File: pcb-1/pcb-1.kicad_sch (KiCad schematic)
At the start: 6 parts, among them J1 Raspberry_Pi_2_3, J2 Screw_Terminal_01x03, J3 Conn_01x07_Socket, J4 Screw_Terminal_01x02, U1 Pico

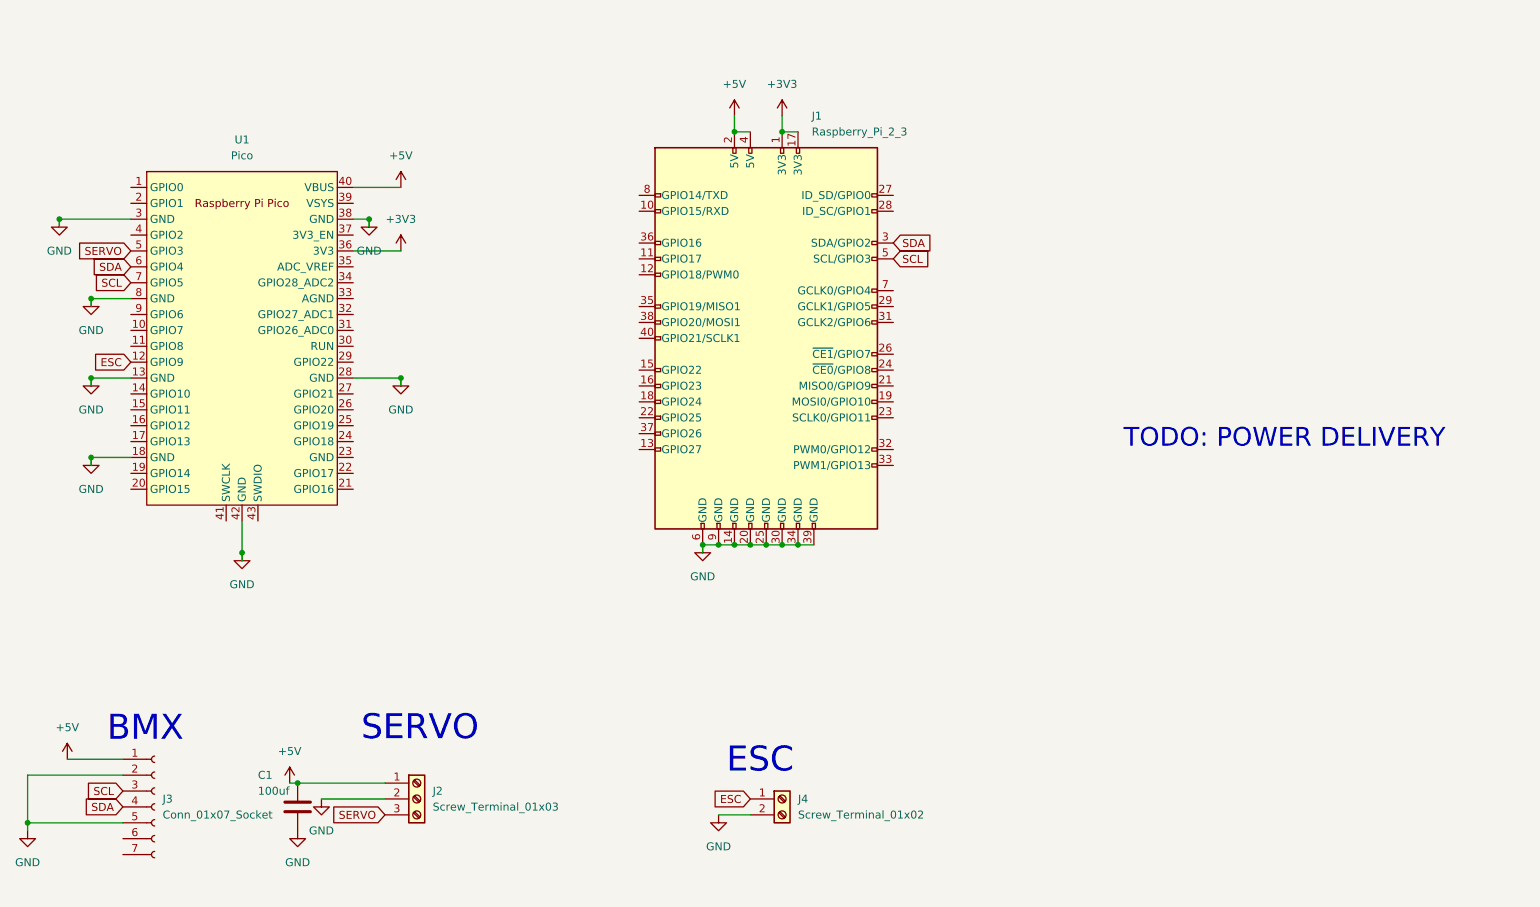
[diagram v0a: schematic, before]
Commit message: updated directory naming, completed routing? (still unsure about decoupling cap location)
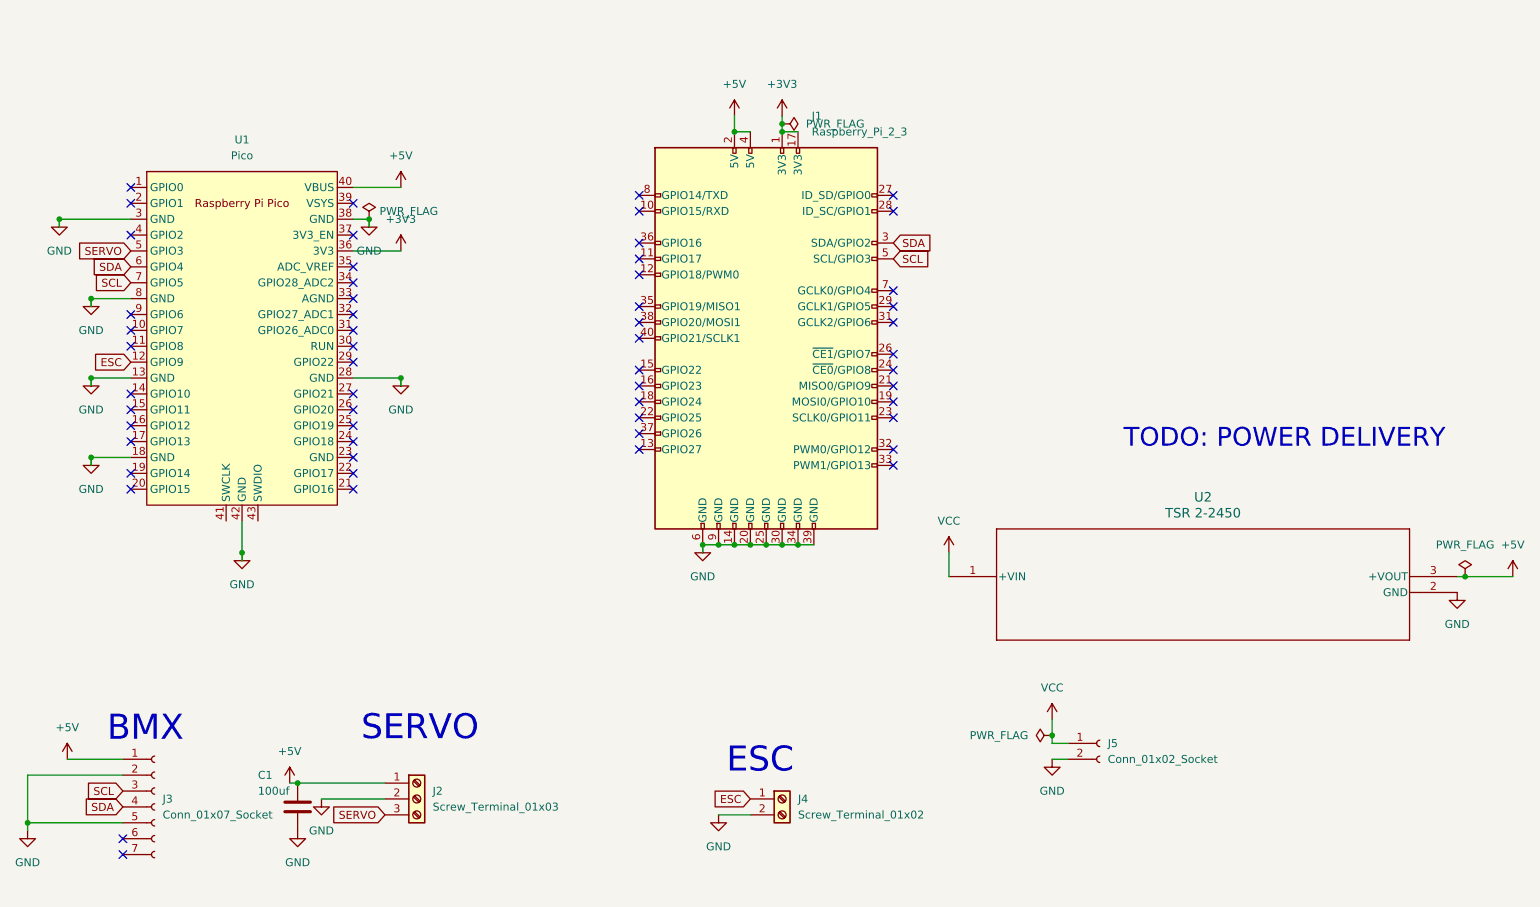
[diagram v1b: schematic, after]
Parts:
- added J5: Conn_01x02_Socket, Connector_AMASS:AMASS_XT60-F_1x02_P7.20mm_Vertical, symbol Connector:Conn_01x02_Socket
- added U2: TSR 2-2450, txr:TSR 2-2450_TRP, symbol txr:TSR_2-2450
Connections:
- net +5V: now also U2.3 (+VOUT)
- net GND: now also J5.2 (Pin_2), U2.2 (GND)
- new net VCC: J5.1 (Pin_1), U2.1 (+VIN)
- no-connect marks 0 -> 56

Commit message: removed bad 3v3 net, adjusted dimensions
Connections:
- removed net +3V3: J1.1 (3V3), J1.17 (3V3), U1.36 (3V3)
- no-connect marks 56 -> 59
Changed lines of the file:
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@@
   (junction (at 54.61 109.22) (diameter 0) (color 0 0 0 0)
   )
-  (junction (at 165.1 55.88) (diameter 0) (color 0 0 0 0)
-  )
   (junction (at 162.56 123.19) (diameter 0) (color 0 0 0 0)
   )
@@
   (junction (at 78.74 124.46) (diameter 0) (color 0 0 0 0)
   )
-  (junction (at 165.1 57.15) (diameter 0) (color 0 0 0 0)
-  )
   (junction (at 160.02 123.19) (diameter 0) (color 0 0 0 0)
   )
@@
   )
   (no_connect (at 96.52 109.22))
+  (no_connect (at 165.1 57.15))
   (no_connect (at 60.96 73.66))
   (no_connect (at 142.24 105.41))
@@
   (no_connect (at 60.96 86.36))
   (no_connect (at 60.96 99.06))
+  (no_connect (at 96.52 76.2))
   (no_connect (at 96.52 91.44))
+  (no_connect (at 167.64 57.15))
   (no_connect (at 60.96 104.14))
   (no_connect (at 182.88 85.09))
@@
     (stroke (width 0) (type default))
   )
-  (wire (pts (xy 165.1 54.61) (xy 165.1 55.88))
-    (stroke (width 0) (type default))
-  )
   (wire (pts (xy 152.4 123.19) (xy 154.94 123.19))
     (stroke (width 0) (type default))
@@
     (stroke (width 0) (type default))
   )
-  (wire (pts (xy 165.1 55.88) (xy 165.1 57.15))
-    (stroke (width 0) (type default))
-  )
-  (wire (pts (xy 96.52 76.2) (xy 104.14 76.2))
-    (stroke (width 0) (type default))
-  )
   (wire (pts (xy 96.52 71.12) (xy 99.06 71.12))
-    (stroke (width 0) (type default))
-  )
-  (wire (pts (xy 165.1 57.15) (xy 167.64 57.15))
     (stroke (width 0) (type default))
   )
@@
     )
   )
-  (symbol (lib_id "power:+3V3") (at 165.1 54.61 0) (unit 1)
-    (in_bom yes) (on_board yes) (dnp no) (fields_autoplaced)
-    (property "Reference" "#PWR012" (at 165.1 58.42 0)
-      (effects (font (size 1.27 1.27)) hide)
-    )
-    (property "Value" "+3V3" (at 165.1 49.53 0)
-      (effects (font (size 1.27 1.27)))
-    )
-    (property "Footprint" "" (at 165.1 54.61 0)
-      (effects (font (size 1.27 1.27)) hide)
-    )
-    (property "Datasheet" "" (at 165.1 54.61 0)
-      (effects (font (size 1.27 1.27)) hide)
-    )
-    (pin "1")
-    (instances
-      (project "pcb-1"
-        (path "/43486df0-1e41-4516-8027-8058a2e1c66f"
-          (reference "#PWR012") (unit 1)
-        )
-      )
-    )
-  )
   (symbol (lib_id "power:VCC") (at 191.77 124.46 0) (unit 1)
     (in_bom yes) (on_board yes) (dnp no) (fields_autoplaced)
@@
     )
   )
-  (symbol (lib_id "power:+3V3") (at 104.14 76.2 0) (unit 1)
-    (in_bom yes) (on_board yes) (dnp no) (fields_autoplaced)
-    (property "Reference" "#PWR01" (at 104.14 80.01 0)
-      (effects (font (size 1.27 1.27)) hide)
-    )
-    (property "Value" "+3V3" (at 104.14 71.12 0)
-      (effects (font (size 1.27 1.27)))
-    )
-    (property "Footprint" "" (at 104.14 76.2 0)
-      (effects (font (size 1.27 1.27)) hide)
-    )
-    (property "Datasheet" "" (at 104.14 76.2 0)
-      (effects (font (size 1.27 1.27)) hide)
-    )
-    (pin "1")
-    (instances
-      (project "pcb-1"
-        (path "/43486df0-1e41-4516-8027-8058a2e1c66f"
-          (reference "#PWR01") (unit 1)
-        )
-      )
-    )
-  )
   (symbol (lib_id "power:VCC") (at 208.28 151.13 0) (unit 1)
     (in_bom yes) (on_board yes) (dnp no) (fields_autoplaced)
@@
         (path "/43486df0-1e41-4516-8027-8058a2e1c66f"
           (reference "#PWR04") (unit 1)
-        )
-      )
-    )
-  )
-  (symbol (lib_id "power:PWR_FLAG") (at 165.1 55.88 270) (unit 1)
-    (in_bom yes) (on_board yes) (dnp no) (fields_autoplaced)
-    (property "Reference" "#FLG02" (at 167.005 55.88 0)
-      (effects (font (size 1.27 1.27)) hide)
-    )
-    (property "Value" "PWR_FLAG" (at 168.91 55.88 90)
-      (effects (font (size 1.27 1.27)) (justify left))
-    )
-    (property "Footprint" "" (at 165.1 55.88 0)
-      (effects (font (size 1.27 1.27)) hide)
-    )
-    (property "Datasheet" "~" (at 165.1 55.88 0)
-      (effects (font (size 1.27 1.27)) hide)
-    )
-    (pin "1")
-    (instances
-      (project "pcb-1"
-        (path "/43486df0-1e41-4516-8027-8058a2e1c66f"
-          (reference "#FLG02") (unit 1)
         )
       )
@@
     )
     (property "Value" "GND" (at 99.06 76.2 0)
-      (effects (font (size 1.27 1.27)))
+      (effects (font (size 1.27 1.27)) hide)
     )
     (property "Footprint" "" (at 99.06 71.12 0)

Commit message: updates to pcb
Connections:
- net +5V: now also J3.7 (Pin_7); no longer J3.1 (Pin_1)
- net GND: now also J3.3 (Pin_3), J3.6 (Pin_6); no longer J3.2 (Pin_2), J3.5 (Pin_5)
- net SCL: now also J3.5 (Pin_5); no longer J3.3 (Pin_3)
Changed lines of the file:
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@@
   (junction (at 54.61 83.82) (diameter 0) (color 0 0 0 0)
   )
-  (junction (at 44.45 167.64) (diameter 0) (color 0 0 0 0)
-  )
   (junction (at 99.06 71.12) (diameter 0) (color 0 0 0 0)
   )
@@
   )
   (junction (at 274.32 128.27) (diameter 0) (color 0 0 0 0)
+  )
+  (junction (at 44.45 170.18) (diameter 0) (color 0 0 0 0)
   )
   (junction (at 167.64 123.19) (diameter 0) (color 0 0 0 0)
@@
   (no_connect (at 142.24 105.41))
   (no_connect (at 96.52 111.76))
+  (no_connect (at 59.69 157.48))
   (no_connect (at 182.88 69.85))
   (no_connect (at 142.24 69.85))
@@
   (no_connect (at 142.24 97.79))
   (no_connect (at 60.96 86.36))
+  (no_connect (at 59.69 160.02))
   (no_connect (at 60.96 99.06))
   (no_connect (at 96.52 76.2))
@@
   (no_connect (at 142.24 77.47))
   (no_connect (at 142.24 85.09))
-  (no_connect (at 59.69 172.72))
   (no_connect (at 96.52 78.74))
   (no_connect (at 182.88 107.95))
@@
   (no_connect (at 142.24 87.63))
   (no_connect (at 96.52 114.3))
-  (no_connect (at 59.69 170.18))
   (no_connect (at 142.24 100.33))
   (no_connect (at 142.24 67.31))
@@
     (stroke (width 0) (type default))
   )
-  (wire (pts (xy 50.8 157.48) (xy 59.69 157.48))
-    (stroke (width 0) (type default))
-  )
   (wire (pts (xy 96.52 66.04) (xy 104.14 66.04))
     (stroke (width 0) (type default))
   )
-  (wire (pts (xy 44.45 160.02) (xy 59.69 160.02))
-    (stroke (width 0) (type default))
-  )
   (wire (pts (xy 152.4 123.19) (xy 152.4 124.46))
     (stroke (width 0) (type default))
@@
     (stroke (width 0) (type default))
   )
-  (wire (pts (xy 44.45 160.02) (xy 44.45 167.64))
-    (stroke (width 0) (type default))
-  )
   (wire (pts (xy 99.06 71.12) (xy 99.06 72.39))
     (stroke (width 0) (type default))
   )
-  (wire (pts (xy 44.45 167.64) (xy 59.69 167.64))
+  (wire (pts (xy 44.45 170.18) (xy 59.69 170.18))
     (stroke (width 0) (type default))
   )
@@
     (stroke (width 0) (type default))
   )
-  (wire (pts (xy 44.45 168.91) (xy 44.45 167.64))
+  (wire (pts (xy 44.45 172.72) (xy 44.45 170.18))
     (stroke (width 0) (type default))
   )
@@
     (stroke (width 0) (type default))
   )
+  (wire (pts (xy 44.45 162.56) (xy 44.45 170.18))
+    (stroke (width 0) (type default))
+  )
   (wire (pts (xy 273.05 128.27) (xy 274.32 128.27))
     (stroke (width 0) (type default))
@@
     (stroke (width 0) (type default))
   )
+  (wire (pts (xy 59.69 177.8) (xy 59.69 172.72))
+    (stroke (width 0) (type default))
+  )
+  (wire (pts (xy 44.45 162.56) (xy 59.69 162.56))
+    (stroke (width 0) (type default))
+  )
   (wire (pts (xy 191.77 124.46) (xy 191.77 128.27))
+    (stroke (width 0) (type default))
+  )
+  (wire (pts (xy 52.07 177.8) (xy 59.69 177.8))
     (stroke (width 0) (type default))
   )
@@
     )
   )
-  (global_label "SCL" (shape input) (at 59.69 162.56 180) (fields_autoplaced)
-    (effects (font (size 1.27 1.27)) (justify right))
-    (property "Intersheetrefs" "${INTERSHEET_REFS}" (at 53.1972 162.56 0)
-      (effects (font (size 1.27 1.27)) (justify right) hide)
-    )
-  )
   (global_label "ESC" (shape input) (at 160.02 163.83 180) (fields_autoplaced)
     (effects (font (size 1.27 1.27)) (justify right))
@@
     )
   )
+  (global_label "SDA" (shape input) (at 59.69 165.1 180) (fields_autoplaced)
+    (effects (font (size 1.27 1.27)) (justify right))
+    (property "Intersheetrefs" "${INTERSHEET_REFS}" (at 53.1367 165.1 0)
+      (effects (font (size 1.27 1.27)) (justify right) hide)
+    )
+  )
   (global_label "SDA" (shape input) (at 182.88 74.93 0) (fields_autoplaced)
     (effects (font (size 1.27 1.27)) (justify left))
@@
     )
   )
-  (global_label "SDA" (shape input) (at 59.69 165.1 180) (fields_autoplaced)
-    (effects (font (size 1.27 1.27)) (justify right))
-    (property "Intersheetrefs" "${INTERSHEET_REFS}" (at 53.1367 165.1 0)
-      (effects (font (size 1.27 1.27)) (justify right) hide)
-    )
-  )
   (global_label "SCL" (shape input) (at 60.96 81.28 180) (fields_autoplaced)
     (effects (font (size 1.27 1.27)) (justify right))
@@
     (effects (font (size 1.27 1.27)) (justify right))
     (property "Intersheetrefs" "${INTERSHEET_REFS}" (at 92.5672 166.37 0)
+      (effects (font (size 1.27 1.27)) (justify right) hide)
+    )
+  )
+  (global_label "SCL" (shape input) (at 59.69 167.64 180) (fields_autoplaced)
+    (effects (font (size 1.27 1.27)) (justify right))
+    (property "Intersheetrefs" "${INTERSHEET_REFS}" (at 53.1972 167.64 0)
       (effects (font (size 1.27 1.27)) (justify right) hide)
     )
@@
         (path "/43486df0-1e41-4516-8027-8058a2e1c66f"
           (reference "#PWR022") (unit 1)
-        )
-      )
-    )
-  )
-  (symbol (lib_id "power:+5V") (at 50.8 157.48 0) (unit 1)
-    (in_bom yes) (on_board yes) (dnp no) (fields_autoplaced)
-    (property "Reference" "#PWR016" (at 50.8 161.29 0)
-      (effects (font (size 1.27 1.27)) hide)
-    )
-    (property "Value" "+5V" (at 50.8 152.4 0)
-      (effects (font (size 1.27 1.27)))
-    )
-    (property "Footprint" "" (at 50.8 157.48 0)
-      (effects (font (size 1.27 1.27)) hide)
-    )
-    (property "Datasheet" "" (at 50.8 157.48 0)
-      (effects (font (size 1.27 1.27)) hide)
-    )
-    (pin "1")
-    (instances
-      (project "pcb-1"
-        (path "/43486df0-1e41-4516-8027-8058a2e1c66f"
-          (reference "#PWR016") (unit 1)
         )
       )
@@
     )
   )
-  (symbol (lib_id "power:GND") (at 44.45 168.91 0) (unit 1)
-    (in_bom yes) (on_board yes) (dnp no) (fields_autoplaced)
-    (property "Reference" "#PWR014" (at 44.45 175.26 0)
-      (effects (font (size 1.27 1.27)) hide)
-    )
-    (property "Value" "GND" (at 44.45 173.99 0)
-      (effects (font (size 1.27 1.27)))
-    )
-    (property "Footprint" "" (at 44.45 168.91 0)
-      (effects (font (size 1.27 1.27)) hide)
-    )
-    (property "Datasheet" "" (at 44.45 168.91 0)
+  (symbol (lib_id "power:GND") (at 44.45 172.72 0) (unit 1)
+    (in_bom yes) (on_board yes) (dnp no) (fields_autoplaced)
+    (property "Reference" "#PWR014" (at 44.45 179.07 0)
+      (effects (font (size 1.27 1.27)) hide)
+    )
+    (property "Value" "GND" (at 44.45 177.8 0)
+      (effects (font (size 1.27 1.27)))
+    )
+    (property "Footprint" "" (at 44.45 172.72 0)
+      (effects (font (size 1.27 1.27)) hide)
+    )
+    (property "Datasheet" "" (at 44.45 172.72 0)
       (effects (font (size 1.27 1.27)) hide)
     )
@@
         )
       )
+    )
+  )
+  (symbol (lib_id "power:+5V") (at 52.07 177.8 0) (unit 1)
+    (in_bom yes) (on_board yes) (dnp no) (fields_autoplaced)
+    (property "Reference" "#PWR01" (at 52.07 181.61 0)
+      (effects (font (size 1.27 1.27)) hide)
+    )
+    (property "Value" "+5V" (at 52.07 172.72 0)
+      (effects (font (size 1.27 1.27)))
+    )
+    (property "Footprint" "" (at 52.07 177.8 0)
+      (effects (font (size 1.27 1.27)) hide)
+    )
+    (property "Datasheet" "" (at 52.07 177.8 0)
+      (effects (font (size 1.27 1.27)) hide)
+    )
+    (pin "1")
+    (instances
+      (project "pcb-1"
+        (path "/43486df0-1e41-4516-8027-8058a2e1c66f"
+          (reference "#PWR01") (unit 1)
+        )
+      )
